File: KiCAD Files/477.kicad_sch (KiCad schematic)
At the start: 37 parts, among them IC1 W25N01GVSFIG, IC2 W25N01GVSFIG, IC3 W25N01GVSFIG, IC4 W25N01GVSFIG, IC5 AZ1117IH-3.3TRG1, J1 BM06B-SRSS-TBT_LF__SN_, J2 6364372-2, SW1 SW_Push, U1 STM32H7A3RGTx, Y2 ABM8G-48.000MHZ-18-D2Y-T

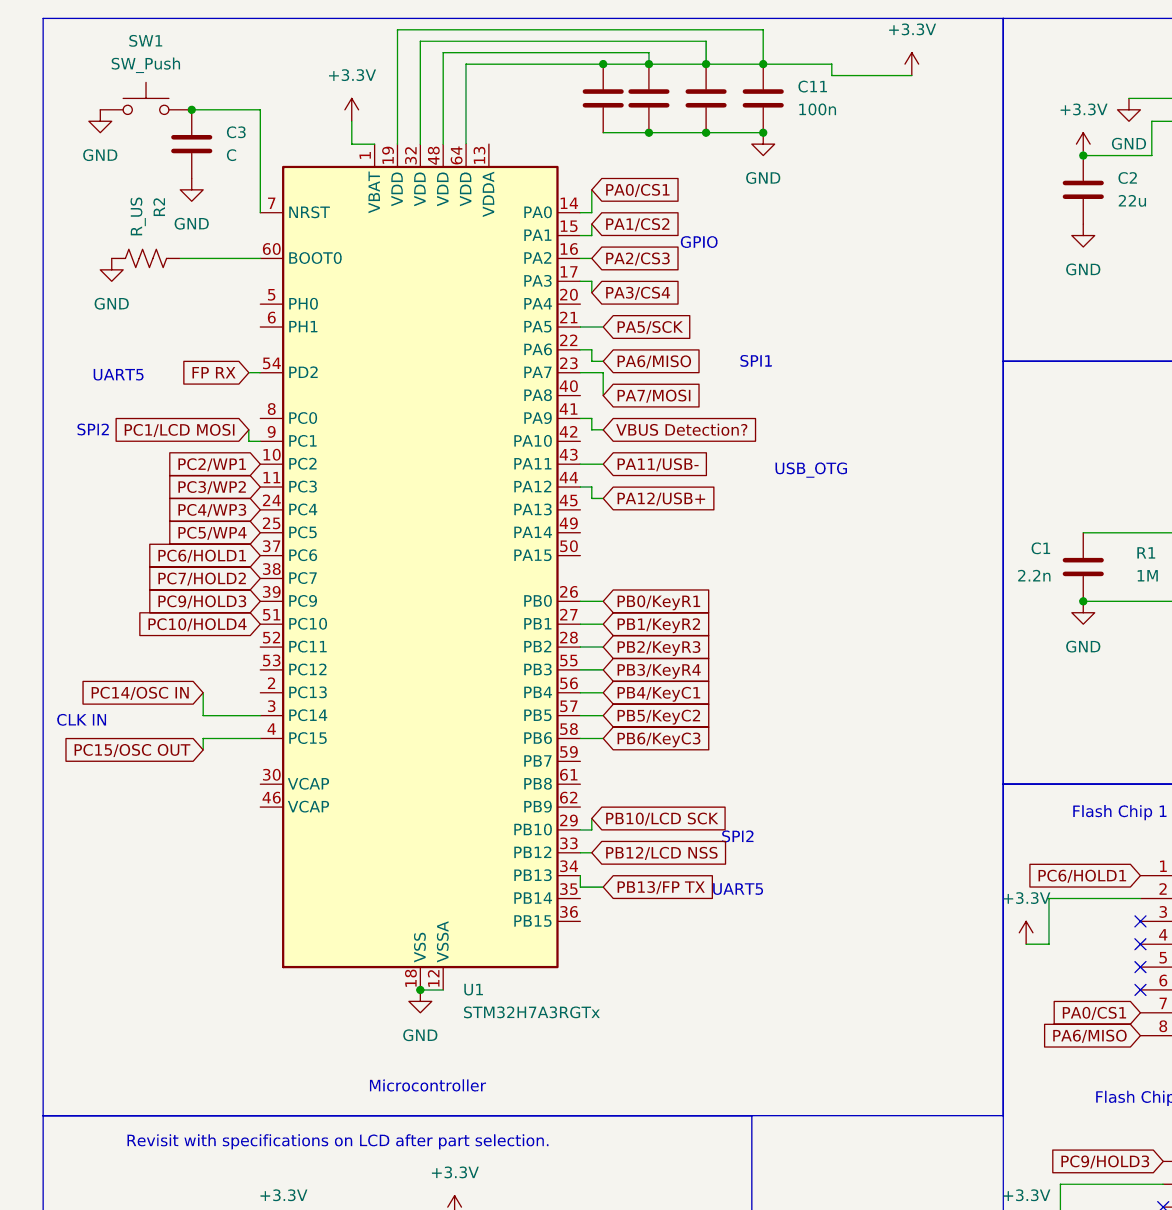
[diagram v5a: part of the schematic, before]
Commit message: added button and tweaked silkscreen
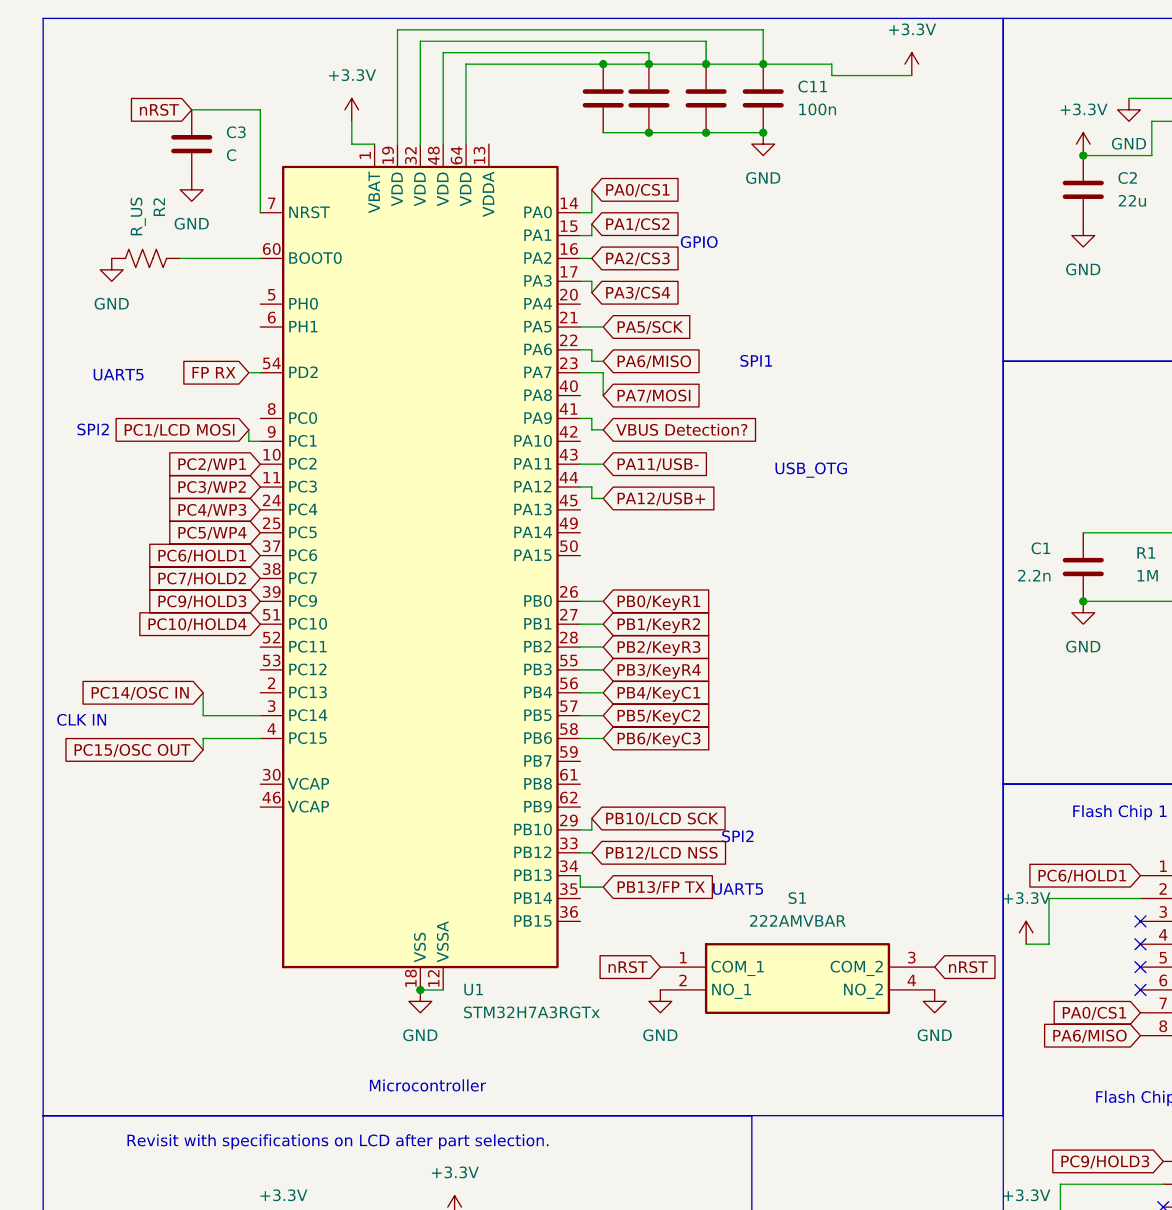
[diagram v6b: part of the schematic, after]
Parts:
- removed SW1: SW_Push, symbol Switch:SW_Push
- added S1: 222AMVBAR, CustomFootprints:custom, symbol CustomSymbols:222AMVBAR
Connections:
- net GND: now also S1.2 (NO_1), S1.4 (NO_2)
- net nRST: now reaches C3.1, U1.7 (NRST)
- net nRST: now also S1.1 (COM_1), S1.3 (COM_2)

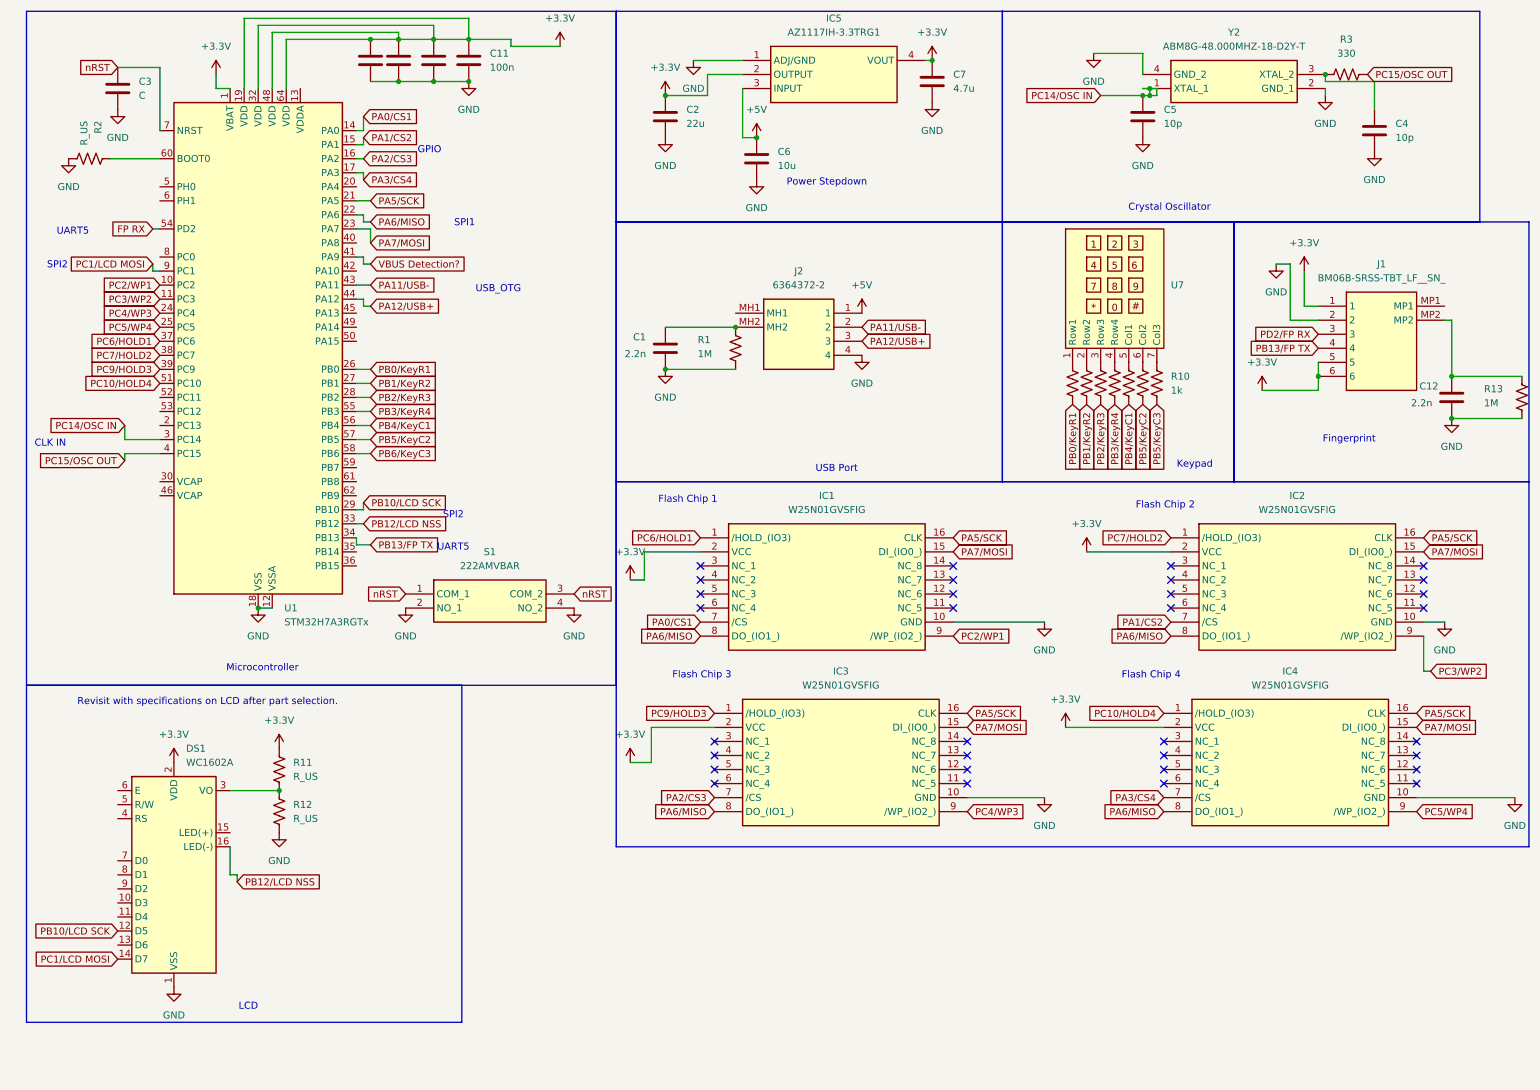
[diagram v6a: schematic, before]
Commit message: tweaked pcb and schematics with micro power wiring and debugging additions
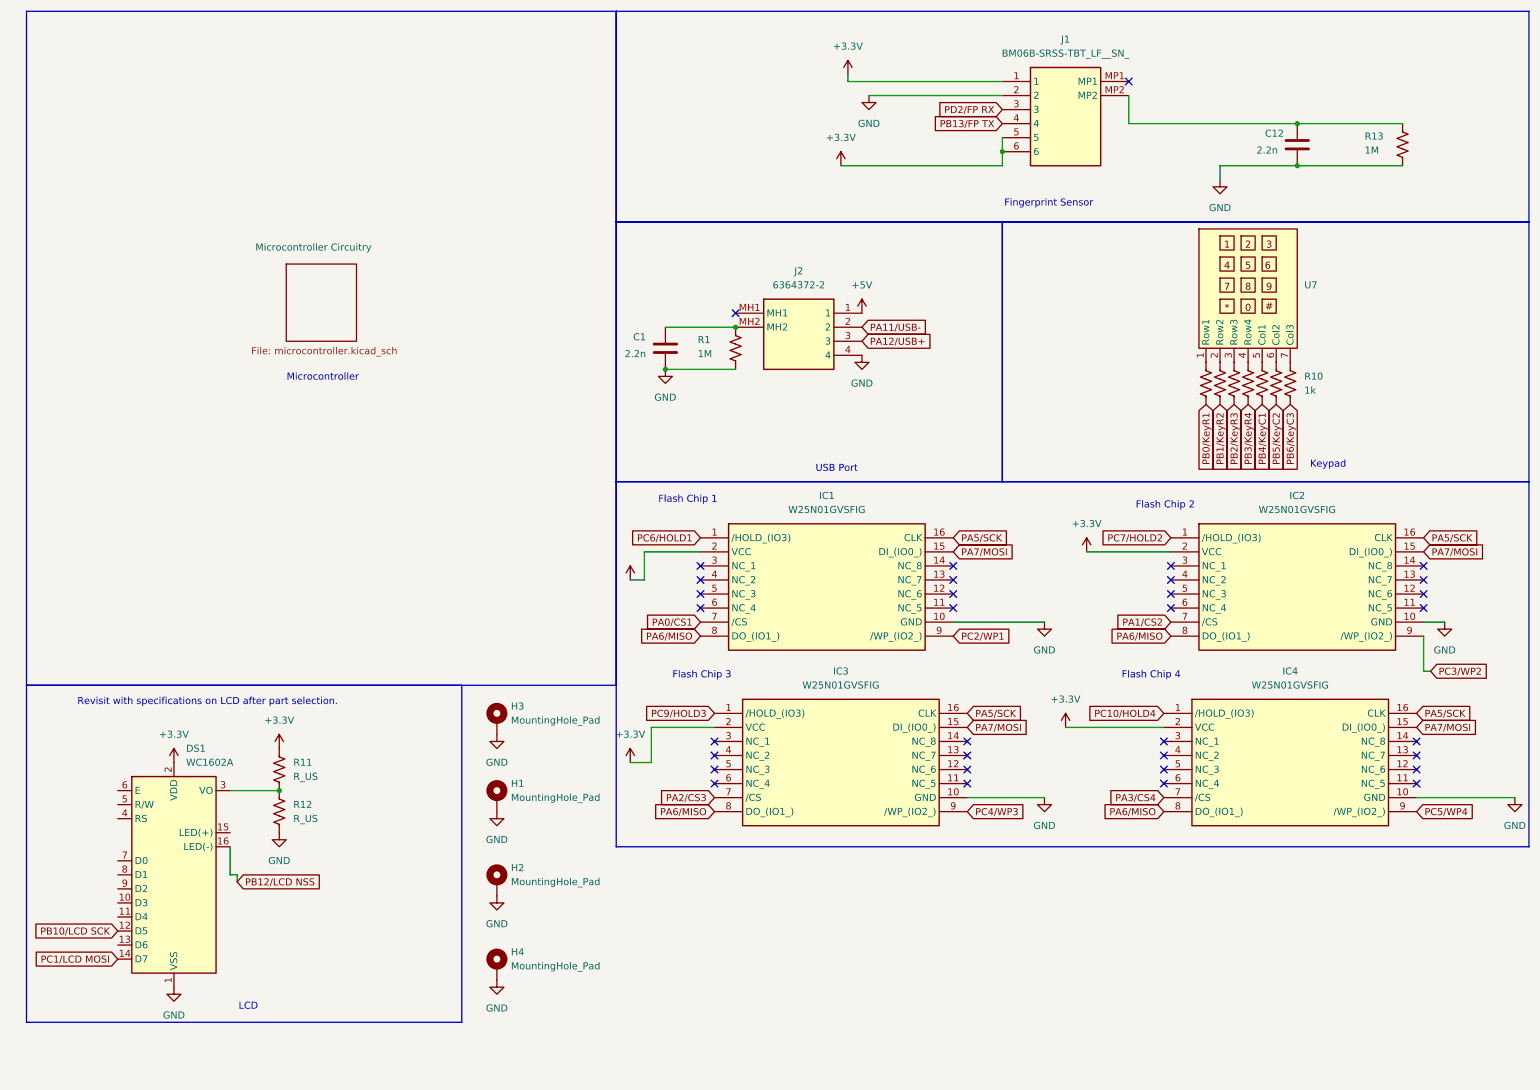
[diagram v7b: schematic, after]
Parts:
- removed C10, C11, C8, C9: 100n, Capacitor_SMD:C_0805_2012Metric_Pad1.18x1.45mm_HandSolder, symbol CustomSymbols:C
- removed C2: 22u, Capacitor_SMD:C_0805_2012Metric_Pad1.18x1.45mm_HandSolder, symbol CustomSymbols:C
- removed C3: C, Capacitor_SMD:C_0805_2012Metric_Pad1.18x1.45mm_HandSolder, symbol CustomSymbols:C
- removed C4, C5: 10p, Capacitor_SMD:C_0805_2012Metric_Pad1.18x1.45mm_HandSolder, symbol CustomSymbols:C
- removed C6: 10u, Capacitor_SMD:C_0805_2012Metric_Pad1.18x1.45mm_HandSolder, symbol CustomSymbols:C
- removed C7: 4.7u, Capacitor_SMD:C_0805_2012Metric_Pad1.18x1.45mm_HandSolder, symbol CustomSymbols:C
- removed IC5: AZ1117IH-3.3TRG1, SOT230P700X180-4N, symbol CustomSymbols:AZ1117IH-3.3TRG1
- removed R2: R_US, Resistor_SMD:R_0805_2012Metric_Pad1.20x1.40mm_HandSolder, symbol CustomSymbols:R_US
- removed R3: 330, Resistor_SMD:R_0805_2012Metric_Pad1.20x1.40mm_HandSolder, symbol CustomSymbols:R_US
- removed S1: 222AMVBAR, CustomFootprints:custom, symbol CustomSymbols:222AMVBAR
- removed U1: STM32H7A3RGTx, Package_QFP:LQFP-64_10x10mm_P0.5mm, symbol CustomSymbols:STM32H7A3RGTx
- removed Y2: ABM8G-48.000MHZ-18-D2Y-T, ABM8G, symbol CustomSymbols:ABM8G-48.000MHZ-18-D2Y-T
- added H1, H2, H3, H4: MountingHole_Pad, MountingHole:MountingHole_3.2mm_M3_DIN965_Pad, symbol Mechanical:MountingHole_Pad
- R10: footprint (none) -> Resistor_SMD:R_0805_2012Metric_Pad1.20x1.40mm_HandSolder
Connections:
- net PB5/KeyC3 is gone; now on net PB6/KeyC3: R10.2
- net GND: now also H1.1, H2.1, H3.1, H4.1
- no-connect marks 32 -> 34
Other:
- added sheet Microcontroller Circuitry (microcontroller.kicad_sch)
- note added: "Fingerprint Sensor"
- note removed: "CLK IN"
- note removed: "Crystal Oscillator"
- note removed: "Fingerprint"
- note removed: "GPIO"
- note removed: "Power Stepdown"
- note removed: "SPI1"
- note removed: "SPI2"
- note removed: "UART5"
- note removed: "USB_OTG"
- moved on the sheet: R10, U7

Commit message: tweaked schematic to pass erc
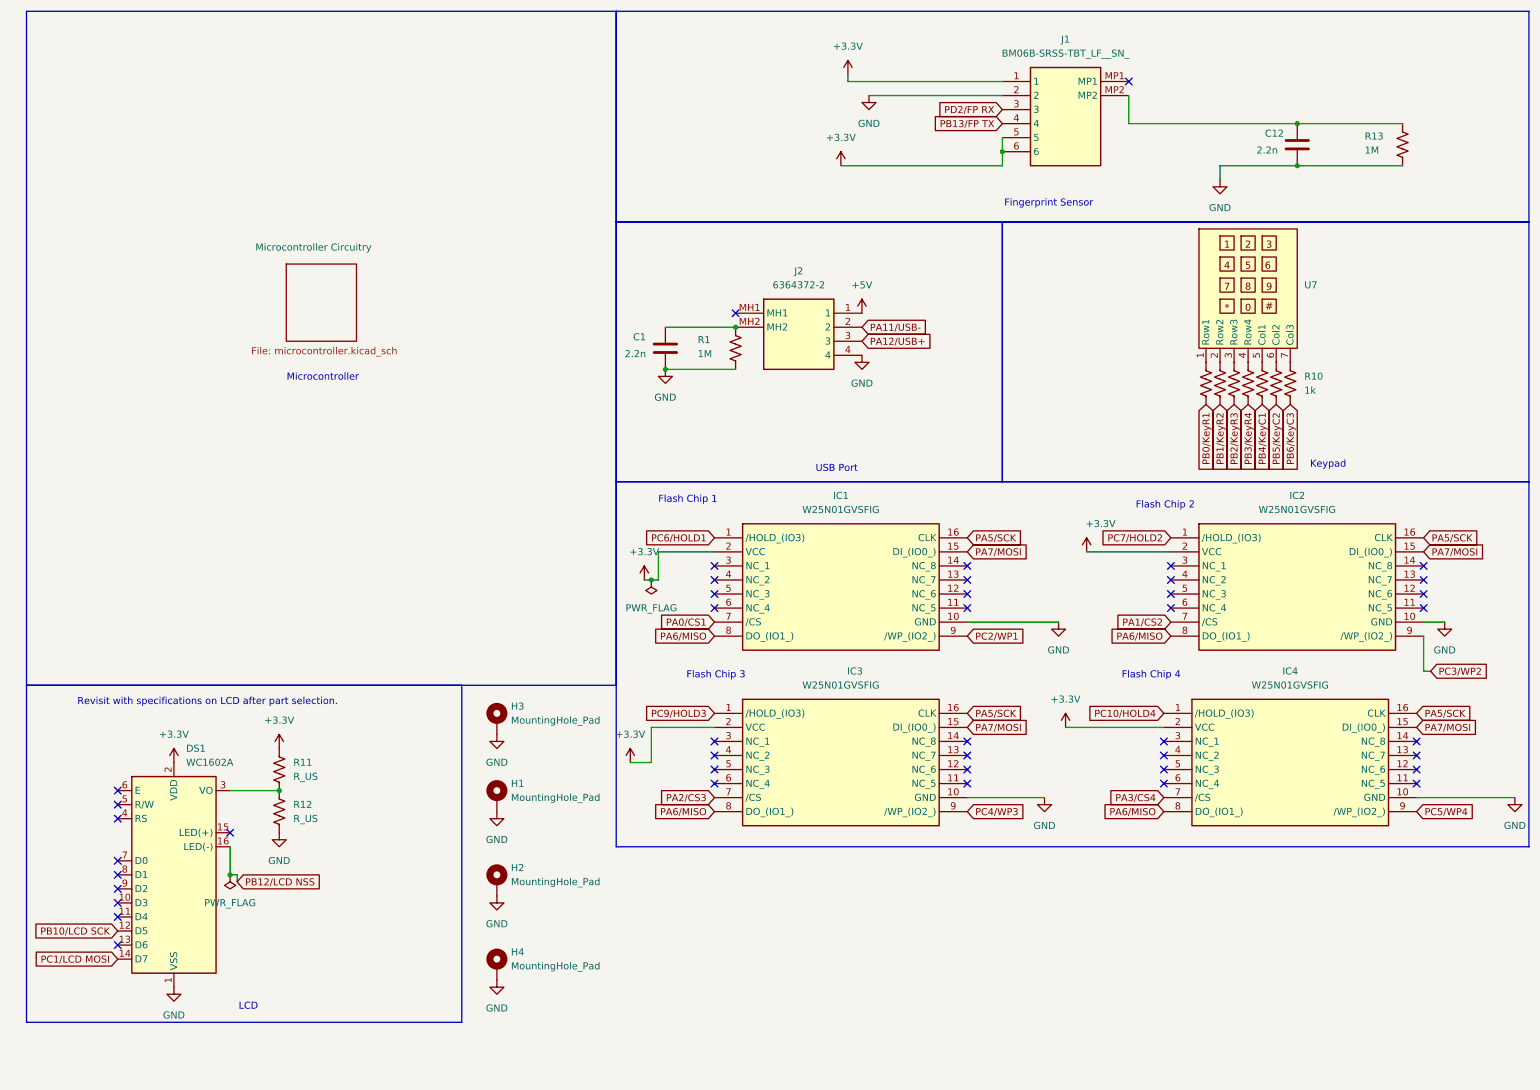
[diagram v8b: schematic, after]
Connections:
- no-connect marks 34 -> 44
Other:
- moved on the sheet: IC1
